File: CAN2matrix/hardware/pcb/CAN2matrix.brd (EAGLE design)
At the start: 41 parts, among them IC1 MEGA8-P, IC2 MCP2515-E/P, IC3 MCP2515-E/P, U1 MCP2551P, U2 MCP2551P, X1 CAN1, X2 CAN2

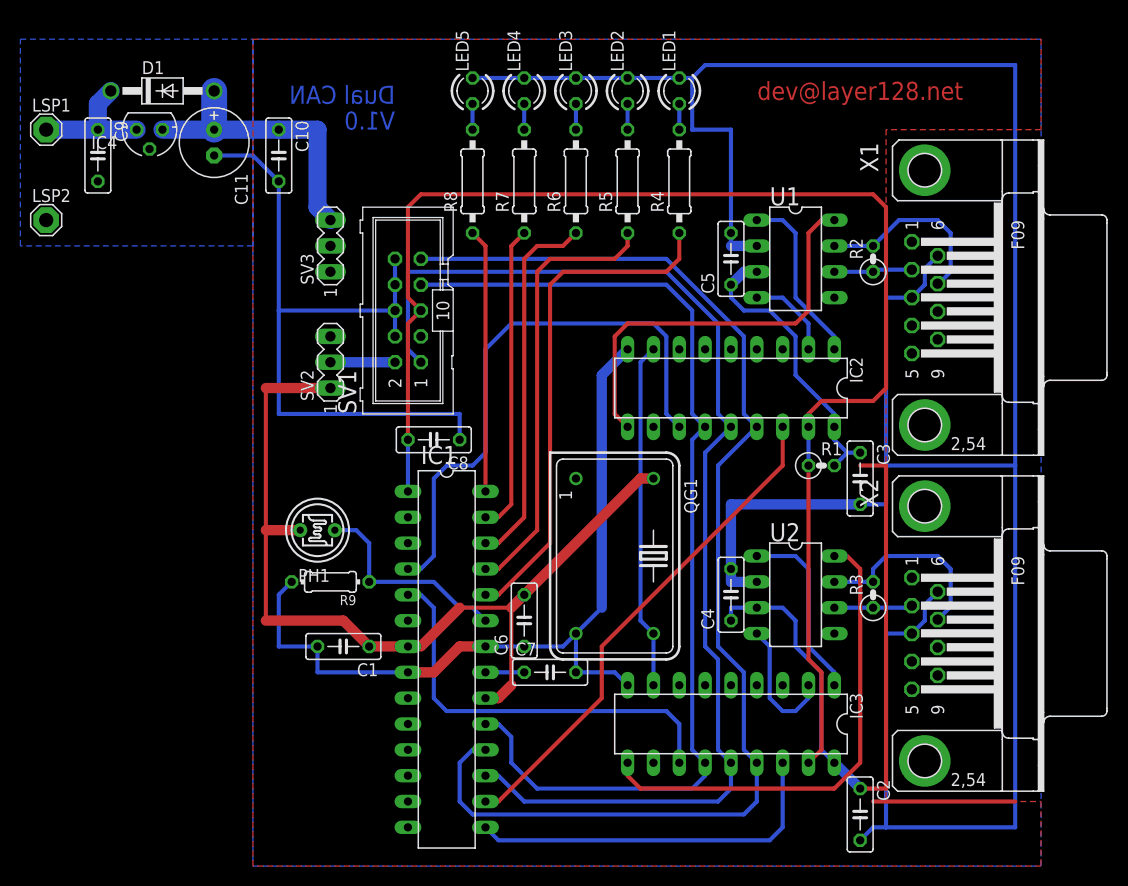
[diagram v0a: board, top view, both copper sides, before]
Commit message: test layout with Design Rules by Eurocircuits and change text to vector graphics - no update on images
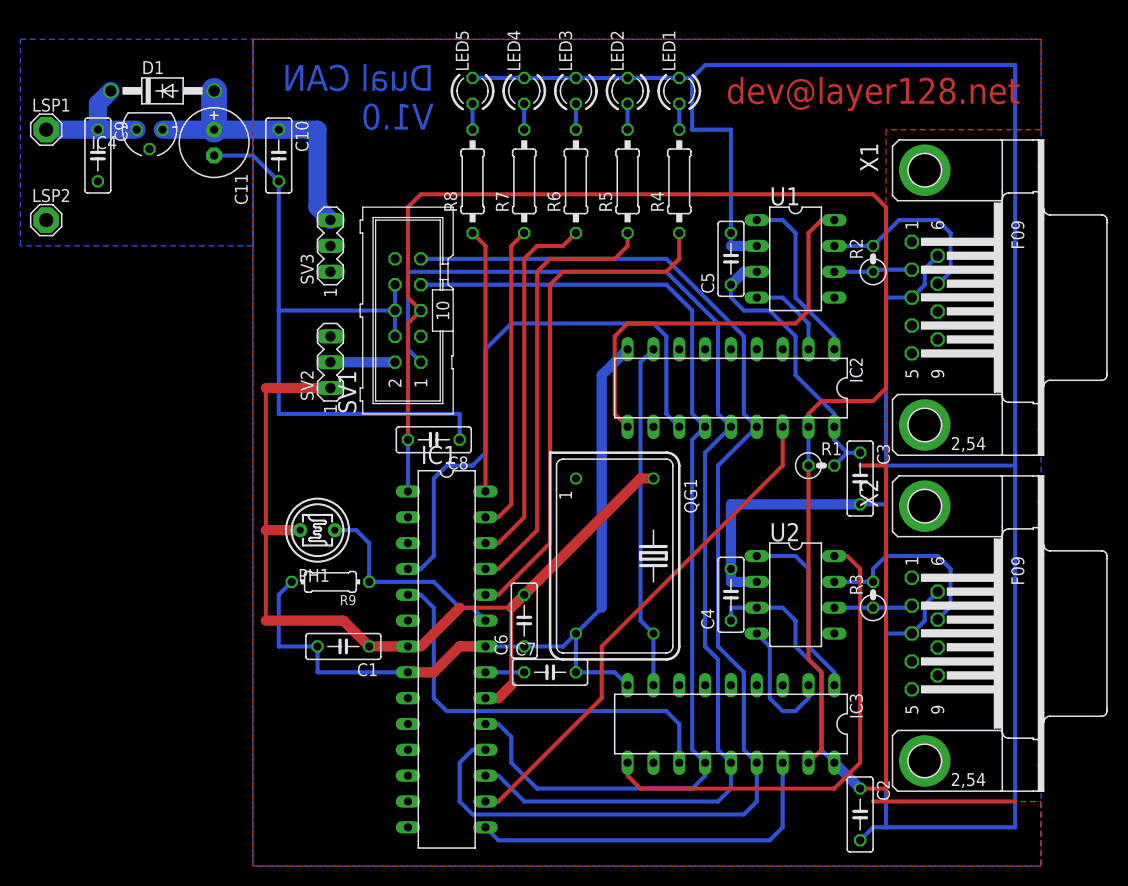
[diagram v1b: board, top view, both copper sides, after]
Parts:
- SV1: value ISP (WSL10G) -> ISP
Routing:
- net GND: track 409.6 -> 407.1 mm
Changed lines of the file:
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@@
 <layers>
 <layer number="1" name="Top" color="4" fill="1" visible="yes" active="yes"/>
-<layer number="16" name="Bottom" color="1" fill="1" visible="no" active="yes"/>
+<layer number="16" name="Bottom" color="1" fill="1" visible="yes" active="yes"/>
 <layer number="17" name="Pads" color="2" fill="1" visible="yes" active="yes"/>
 <layer number="18" name="Vias" color="2" fill="1" visible="yes" active="yes"/>
@@
 <layer number="27" name="tValues" color="7" fill="1" visible="yes" active="yes"/>
 <layer number="28" name="bValues" color="7" fill="1" visible="yes" active="yes"/>
-<layer number="29" name="tStop" color="7" fill="3" visible="no" active="yes"/>
-<layer number="30" name="bStop" color="7" fill="6" visible="no" active="yes"/>
+<layer number="29" name="tStop" color="7" fill="3" visible="yes" active="yes"/>
+<layer number="30" name="bStop" color="7" fill="6" visible="yes" active="yes"/>
 <layer number="31" name="tCream" color="7" fill="4" visible="yes" active="yes"/>
 <layer number="32" name="bCream" color="7" fill="5" visible="yes" active="yes"/>
@@
 <board>
 <plain>
-<text x="36.83" y="74.93" size="1.778" layer="16" rot="MR0">Dual CAN</text>
-<text x="36.83" y="72.39" size="1.778" layer="16" rot="MR0">V1.0</text>
-<text x="82.55" y="76.2" size="1.778" layer="1" align="center">dev@layer128.net</text>
+<text x="40.64" y="76.2" size="2.54" layer="16" font="vector" rot="MR0">Dual CAN</text>
+<text x="40.64" y="72.39" size="2.54" layer="16" font="vector" rot="MR0">V1.0</text>
+<text x="83.82" y="76.2" size="2.54" layer="1" font="vector" align="center">dev@layer128.net</text>
 <rectangle x1="0" y1="0" x2="100.33" y2="81.28" layer="29"/>
 </plain>
@@
 </classes>
 <designrules>
-<description language="de">&lt;b&gt;EAGLE Design Rules&lt;/b&gt;
+<description language="de">&lt;p&gt;
+&lt;b&gt;EAGLE design rules for the Eurocircuits STANDARD pool service 2-layer&lt;/b&gt;
 &lt;p&gt;
-Die Standard-Design-Rules sind so gewählt, dass sie für
-die meisten Anwendungen passen. Sollte ihre Platine
-besondere Anforderungen haben, treffen Sie die erforderlichen
-Einstellungen hier und speichern die Design Rules unter
-einem neuen Namen ab.</description>
-<description language="en">&lt;b&gt;EAGLE Design Rules&lt;/b&gt;
+The design rule parameters in this DRU file have been set to the minimum values compatible with our STANDARD pool service.&lt;br&gt;
+The options &lt;b&gt;Shapes&lt;/b&gt; and &lt;b&gt;Misc&lt;/b&gt; are not relevant.&lt;br&gt;
+Values for &lt;b&gt;Shapes-Smds-Roundness&lt;/b&gt; are not critical and can be set as you require.&lt;br&gt;
+You can set the values for covered or tented via holes under &lt;b&gt;Masks -Limit&lt;/b&gt;.
 &lt;p&gt;
-The default Design Rules have been set to cover
-a wide range of applications. Your particular design
-may have different requirements, so please make the
-necessary adjustments and save your customized
-design rules under a new name.</description>
+You can set larger minimum values if you wish but if you change to smaller minimum values your design cannot be made on the STANDARD pool service.&lt;br&gt;
+If you need smaller values, please use our TECH pool service.
+&lt;p&gt;
+Your Eurocircuits Team</description>
+<description language="en">&lt;p&gt;
+&lt;b&gt;EAGLE design rules for the Eurocircuits STANDARD pool service 2-layer&lt;/b&gt;
+&lt;p&gt;
+The design rule parameters in this DRU file have been set to the minimum values compatible with our STANDARD pool service.&lt;br&gt;
+The options &lt;b&gt;Shapes&lt;/b&gt; and &lt;b&gt;Misc&lt;/b&gt; are not relevant.&lt;br&gt;
+Values for &lt;b&gt;Shapes-Smds-Roundness&lt;/b&gt; are not critical and can be set as you require.&lt;br&gt;
+You can set the values for covered or tented via holes under &lt;b&gt;Masks -Limit&lt;/b&gt;.
+&lt;p&gt;
+You can set larger minimum values if you wish but if you change to smaller minimum values your design cannot be made on the STANDARD pool service.&lt;br&gt;
+If you need smaller values, please use our TECH pool service.
+&lt;p&gt;
+Your Eurocircuits Team</description>
 <param name="layerSetup" value="(1*16)"/>
-<param name="mtCopper" value="0.035mm 0.035mm 0.035mm 0.035mm 0.035mm 0.035mm 0.035mm 0.035mm 0.035mm 0.035mm 0.035mm 0.035mm 0.035mm 0.035mm 0.035mm 0.035mm"/>
-<param name="mtIsolate" value="1.5mm 0.15mm 0.2mm 0.15mm 0.2mm 0.15mm 0.2mm 0.15mm 0.2mm 0.15mm 0.2mm 0.15mm 0.2mm 0.15mm 0.2mm"/>
-<param name="mdWireWire" value="8mil"/>
-<param name="mdWirePad" value="8mil"/>
-<param name="mdWireVia" value="8mil"/>
-<param name="mdPadPad" value="8mil"/>
-<param name="mdPadVia" value="8mil"/>
-<param name="mdViaVia" value="8mil"/>
-<param name="mdSmdPad" value="8mil"/>
-<param name="mdSmdVia" value="8mil"/>
-<param name="mdSmdSmd" value="8mil"/>
-<param name="mdViaViaSameLayer" value="8mil"/>
+<param name="mtCopper" value="0.018mm 0.035mm 0.035mm 0.035mm 0.035mm 0.035mm 0.035mm 0.035mm 0.035mm 0.035mm 0.035mm 0.035mm 0.035mm 0.035mm 0.035mm 0.018mm"/>
+<param name="mtIsolate" value="1.55mm 0.71mm 0.36mm 0.2mm 0.2mm 0.2mm 0.2mm 0.15mm 0.2mm 0.15mm 0.2mm 0.15mm 0.2mm 0.15mm 0.2mm"/>
+<param name="mdWireWire" value="0.15mm"/>
+<param name="mdWirePad" value="0.15mm"/>
+<param name="mdWireVia" value="0.15mm"/>
+<param name="mdPadPad" value="0.15mm"/>
+<param name="mdPadVia" value="0.15mm"/>
+<param name="mdViaVia" value="0.15mm"/>
+<param name="mdSmdPad" value="0.15mm"/>
+<param name="mdSmdVia" value="0.15mm"/>
+<param name="mdSmdSmd" value="0.15mm"/>
+<param name="mdViaViaSameLayer" value="0.2mm"/>
 <param name="mnLayersViaInSmd" value="2"/>
-<param name="mdCopperDimension" value="40mil"/>
-<param name="mdDrill" value="8mil"/>
+<param name="mdCopperDimension" value="0.45mm"/>
+<param name="mdDrill" value="0.3mm"/>
 <param name="mdSmdStop" value="0mil"/>
-<param name="msWidth" value="10mil"/>
-<param name="msDrill" value="24mil"/>
-<param name="msMicroVia" value="9.99mm"/>
+<param name="msWidth" value="0.15mm"/>
+<param name="msDrill" value="0.25mm"/>
+<param name="msMicroVia" value="25mm"/>
 <param name="msBlindViaRatio" value="0.5"/>
-<param name="rvPadTop" value="0.25"/>
-<param name="rvPadInner" value="0.25"/>
-<param name="rvPadBottom" value="0.25"/>
-<param name="rvViaOuter" value="0.25"/>
-<param name="rvViaInner" value="0.25"/>
-<param name="rvMicroViaOuter" value="0.25"/>
-<param name="rvMicroViaInner" value="0.25"/>
-<param name="rlMinPadTop" value="10mil"/>
-<param name="rlMaxPadTop" value="20mil"/>
-<param name="rlMinPadInner" value="10mil"/>
-<param name="rlMaxPadInner" value="20mil"/>
-<param name="rlMinPadBottom" value="10mil"/>
-<param name="rlMaxPadBottom" value="20mil"/>
-<param name="rlMinViaOuter" value="8mil"/>
-<param name="rlMaxViaOuter" value="20mil"/>
-<param name="rlMinViaInner" value="8mil"/>
-<param name="rlMaxViaInner" value="20mil"/>
-<param name="rlMinMicroViaOuter" value="4mil"/>
-<param name="rlMaxMicroViaOuter" value="20mil"/>
-<param name="rlMinMicroViaInner" value="4mil"/>
-<param name="rlMaxMicroViaInner" value="20mil"/>
+<param name="rvPadTop" value="0"/>
+<param name="rvPadInner" value="0"/>
+<param name="rvPadBottom" value="0"/>
+<param name="rvViaOuter" value="0"/>
+<param name="rvViaInner" value="0"/>
+<param name="rvMicroViaOuter" value="0"/>
+<param name="rvMicroViaInner" value="0"/>
+<param name="rlMinPadTop" value="0.2mm"/>
+<param name="rlMaxPadTop" value="2.5mm"/>
+<param name="rlMinPadInner" value="0.25mm"/>
+<param name="rlMaxPadInner" value="2.5mm"/>
+<param name="rlMinPadBottom" value="0.2mm"/>
+<param name="rlMaxPadBottom" value="2.5mm"/>
+<param name="rlMinViaOuter" value="0.2mm"/>
+<param name="rlMaxViaOuter" value="2.5mm"/>
+<param name="rlMinViaInner" value="0.25mm"/>
+<param name="rlMaxViaInner" value="2.5mm"/>
+<param name="rlMinMicroViaOuter" value="2.5mm"/>
+<param name="rlMaxMicroViaOuter" value="25mm"/>
+<param name="rlMinMicroViaInner" value="2.5mm"/>
+<param name="rlMaxMicroViaInner" value="25mm"/>
 <param name="psTop" value="-1"/>
 <param name="psBottom" value="-1"/>
@@
 <param name="psElongationLong" value="100"/>
 <param name="psElongationOffset" value="100"/>
-<param name="mvStopFrame" value="1"/>
+<param name="mvStopFrame" value="0"/>
 <param name="mvCreamFrame" value="0"/>
-<param name="mlMinStopFrame" value="4mil"/>
-<param name="mlMaxStopFrame" value="4mil"/>
+<param name="mlMinStopFrame" value="0.1mm"/>
+<param name="mlMaxStopFrame" value="0.2mm"/>
 <param name="mlMinCreamFrame" value="0mil"/>
-<param name="mlMaxCreamFrame" value="0mil"/>
+<param name="mlMaxCreamFrame" value="0.2mm"/>
 <param name="mlViaStopLimit" value="0mil"/>
 <param name="srRoundness" value="0"/>
 <param name="srMinRoundness" value="0mil"/>
 <param name="srMaxRoundness" value="0mil"/>
-<param name="slThermalIsolate" value="10mil"/>
+<param name="slThermalIsolate" value="0.2mm"/>
 <param name="slThermalsForVias" value="0"/>
 <param name="dpMaxLengthDifference" value="10mm"/>
@@
 <attribute name="OC_FARNELL" value="unknown" x="25.4" y="-26.67" size="1.778" layer="27" rot="R270" display="off"/>
 </element>
-<element name="SV1" library="con-ml" package="ML10" value="ISP (WSL10G)" x="38.1" y="54.61" rot="R90">
+<element name="SV1" library="con-ml" package="ML10" value="ISP" x="38.1" y="54.61" rot="R90">
 <attribute name="OC_NEWARK" value="unknown" x="86.36" y="85.09" size="1.778" layer="27" rot="R90" display="off"/>
 <attribute name="MPN" value="" x="86.36" y="85.09" size="1.778" layer="27" rot="R90" display="off"/>
@@
 <wire x1="69.85" y1="29.21" x2="69.85" y2="27.94" width="1.016" layer="16"/>
 <wire x1="69.85" y1="27.94" x2="72.39" y2="27.94" width="1.016" layer="16"/>
-<wire x1="36.83" y1="59.69" x2="36.83" y2="57.15" width="0.4064" layer="16"/>
 <wire x1="36.83" y1="57.15" x2="36.83" y2="54.61" width="0.4064" layer="16"/>
 <wire x1="25.4" y1="44.45" x2="25.4" y2="54.61" width="0.4064" layer="16"/>
